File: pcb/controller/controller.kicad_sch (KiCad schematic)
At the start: 12 parts, among them J1 USB_C_Receptacle, SW1 SW_Push, SW2 SW_Push, SW3 SW_Push, SW4 SW_Push, SW5 SW_Push, SW6 SW_Push, SW7 SW_Push, SW8 SW_Push

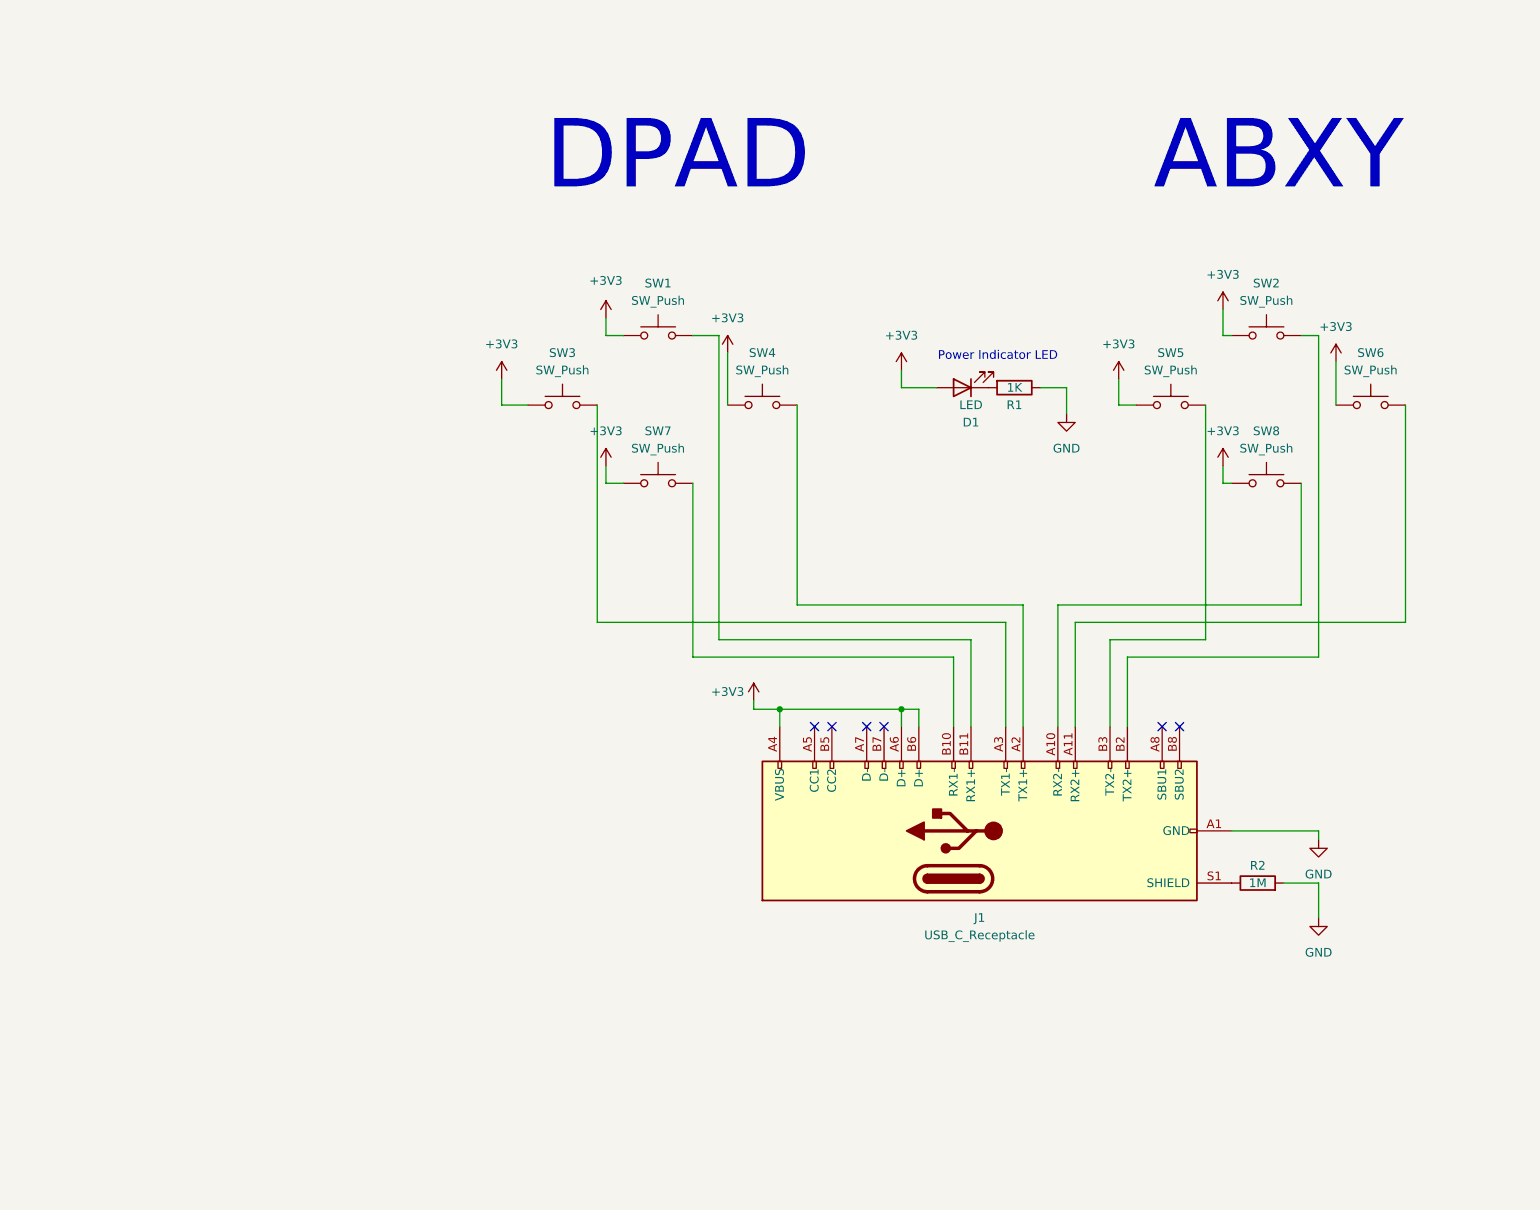
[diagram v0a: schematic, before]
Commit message: Controller rev 2
 - Using an attiny24 and I2C now to communicate between the mainboard and the controllers
   - Gets rid of the massive multiplexer on the mainboard, simplifies things
   - Attiny software will probably be written in arduino because I'm lazy
 - Swapped the connector for a cheaper one since we don't need all 24 pins, still using usb-c though
 - Button layout stays the same
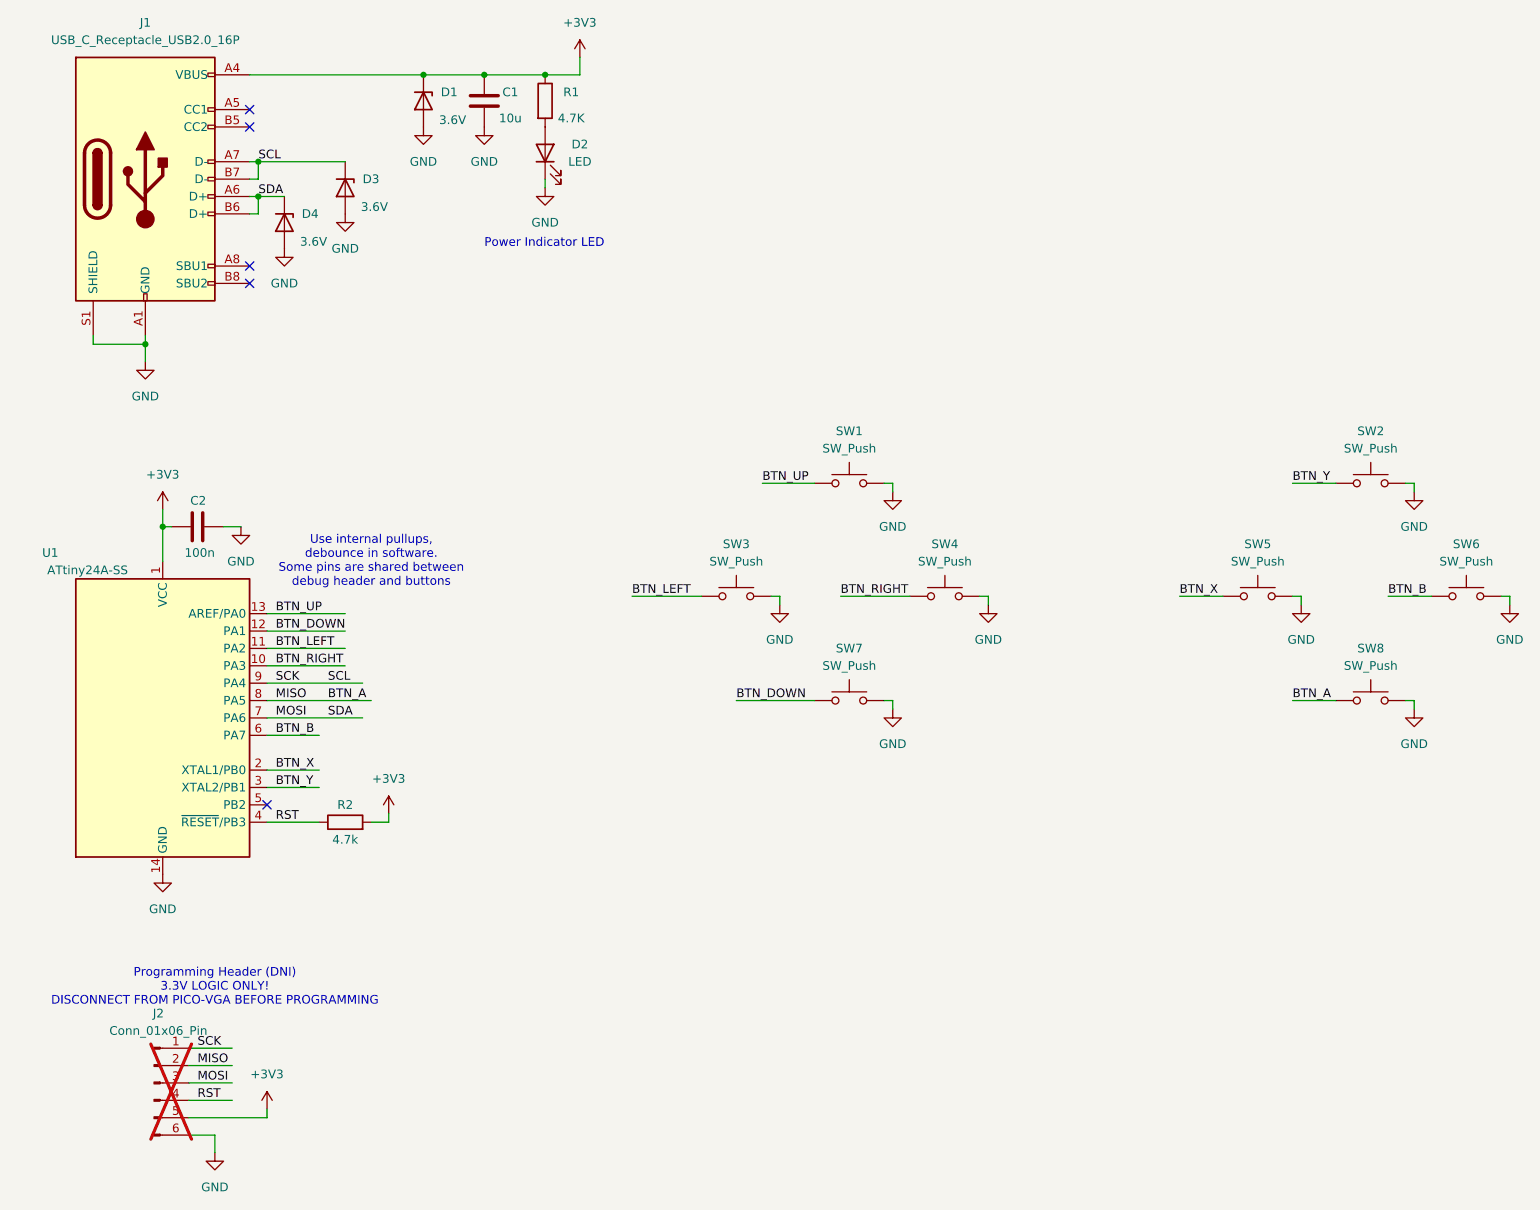
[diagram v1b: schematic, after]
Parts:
- removed D1: LED, LED_SMD:LED_0805_2012Metric_Pad1.15x1.40mm_HandSolder, symbol Device:LED
- removed J1: USB_C_Receptacle, controller:USB_C_Receptacle_Molex_2171830001, symbol Connector:USB_C_Receptacle
- added C1: 10u, Capacitor_SMD:C_0805_2012Metric_Pad1.18x1.45mm_HandSolder, symbol Device:C
- added C2: 100n, Capacitor_SMD:C_0805_2012Metric_Pad1.18x1.45mm_HandSolder, symbol Device:C
- added D1, D3, D4: 3.6V, Diode_SMD:D_SOD-123, symbol Device:D_Zener
- added D2: LED, LED_SMD:LED_0805_2012Metric_Pad1.15x1.40mm_HandSolder, symbol Device:LED
- added J1: USB_C_Receptacle_USB2.0_16P, controller:USB_C_Receptacle_Molex_2169900003, symbol Connector:USB_C_Receptacle_USB2.0_16P
- added J2: Conn_01x06_Pin, Connector_PinHeader_2.54mm:PinHeader_1x06_P2.54mm_Vertical, symbol Connector:Conn_01x06_Pin
- added U1: ATtiny24A-SS, Package_SO:SOIC-14_3.9x8.7mm_P1.27mm, symbol MCU_Microchip_ATtiny:ATtiny24A-SS
- R1: value 1K -> 4.7K; footprint Resistor_SMD:R_0603_1608Metric_Pad0.98x0.95mm_HandSolder -> Resistor_SMD:R_0805_2012Metric_Pad1.20x1.40mm_HandSolder
- R2: value 1M -> 4.7k; footprint Resistor_SMD:R_0603_1608Metric_Pad0.98x0.95mm_HandSolder -> Resistor_SMD:R_0805_2012Metric_Pad1.20x1.40mm_HandSolder
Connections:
- net +3V3: now also R1.1, R2.2, C1.2, C2.1, D1.1 (K), J1.A4 (VBUS), J1.A9 (VBUS), J1.B4 (VBUS), J1.B9 (VBUS), J2.5 (Pin_5), U1.1 (VCC); no longer SW1.1, SW2.1, SW3.1, SW4.1, SW5.1, SW6.1, SW7.1, SW8.1
- net GND: now also SW1.2, SW2.2, SW3.2, SW4.2, SW5.2, SW6.2, SW7.2, SW8.2, C1.1, C2.2, D1.2 (A), D2.1 (K), D3.2 (A), D4.2 (A), J1.A1 (GND), J1.A12 (GND), J1.B1 (GND), J1.B12 (GND), J1.S1 (SHIELD), J2.6 (Pin_6), U1.14 (GND); no longer R1.1, R2.2
- net at R1.2: now also D2.2 (A)
- net RST: now reaches R2.1
- net RST: now also J2.4 (Pin_4), U1.4 (~{RESET}/PB3)
- new net BTN_A: J2.2 (Pin_2), SW8.1, U1.8 (PA5)
- new net BTN_B: SW6.1, U1.6 (PA7)
- new net BTN_DOWN: SW7.1, U1.12 (PA1)
- new net BTN_LEFT: SW3.1, U1.11 (PA2)
- new net BTN_RIGHT: SW4.1, U1.10 (PA3)
- new net BTN_UP: SW1.1, U1.13 (AREF/PA0)
- new net BTN_X: SW5.1, U1.2 (XTAL1/PB0)
- new net BTN_Y: SW2.1, U1.3 (XTAL2/PB1)
- new net MOSI: D4.1 (K), J1.A6 (D+), J1.B6 (D+), J2.3 (Pin_3), U1.7 (PA6)
- new net SCK: D3.1 (K), J1.A7 (D-), J1.B7 (D-), J2.1 (Pin_1), U1.9 (PA4)
- no-connect marks 6 -> 5
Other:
- note added: "Programming Header (DNI) 3.3V LOGIC ONLY! DISCONNECT FROM PICO-VGA BEFORE PROGRAMMING"
- note added: "Use internal pullups, debounce in software. Some pins are shared between debug header and buttons"
- note removed: "ABXY"
- note removed: "DPAD"
